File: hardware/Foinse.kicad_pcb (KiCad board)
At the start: 4 copper layers, 60 x 60 mm, 73 parts, among them J1 ESQ-110-X-X-D, J2 XT30PW-M, J4 PJ-002AH, J6 JTAG-10 PIN, U1 STM32F072C8Tx, U15 INA239AIDGSR, U16 INA239AIDGSR, U17 LTC4412xS6, U19 TPS56A37RPAR, U2 TLV70433DBVT, U4 TJA1051T-3, U5 TPS563203

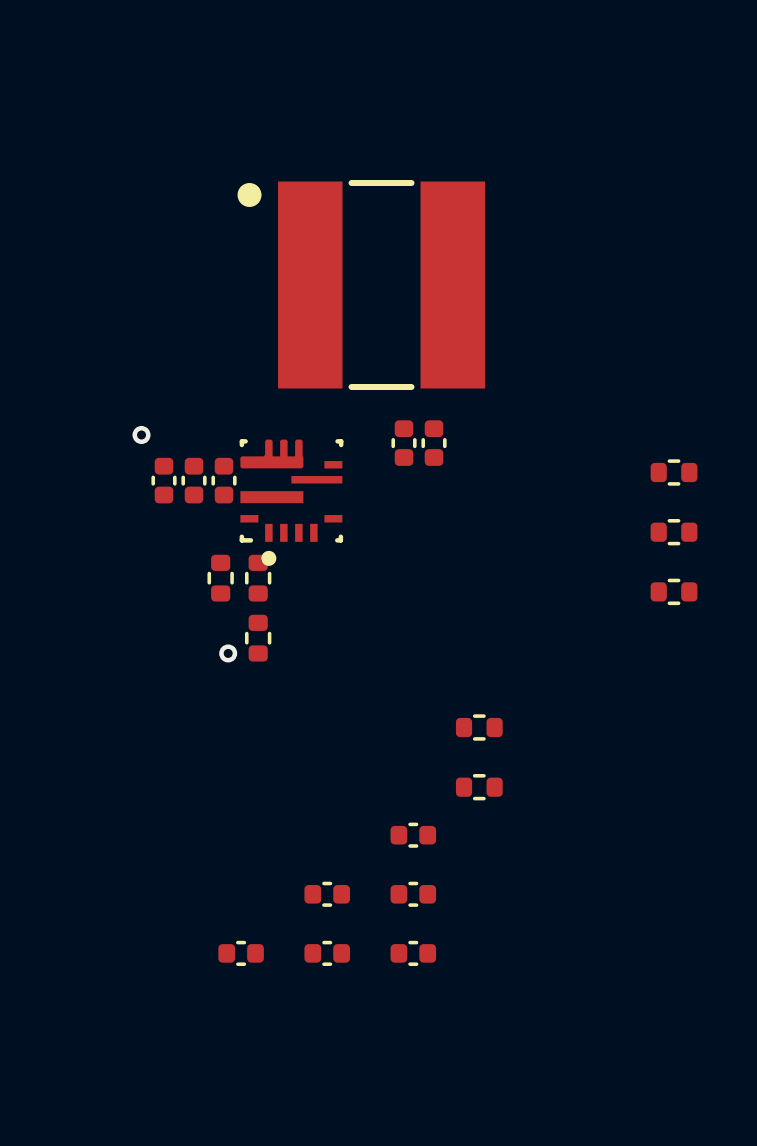
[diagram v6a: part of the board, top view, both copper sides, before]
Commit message: new inductor3
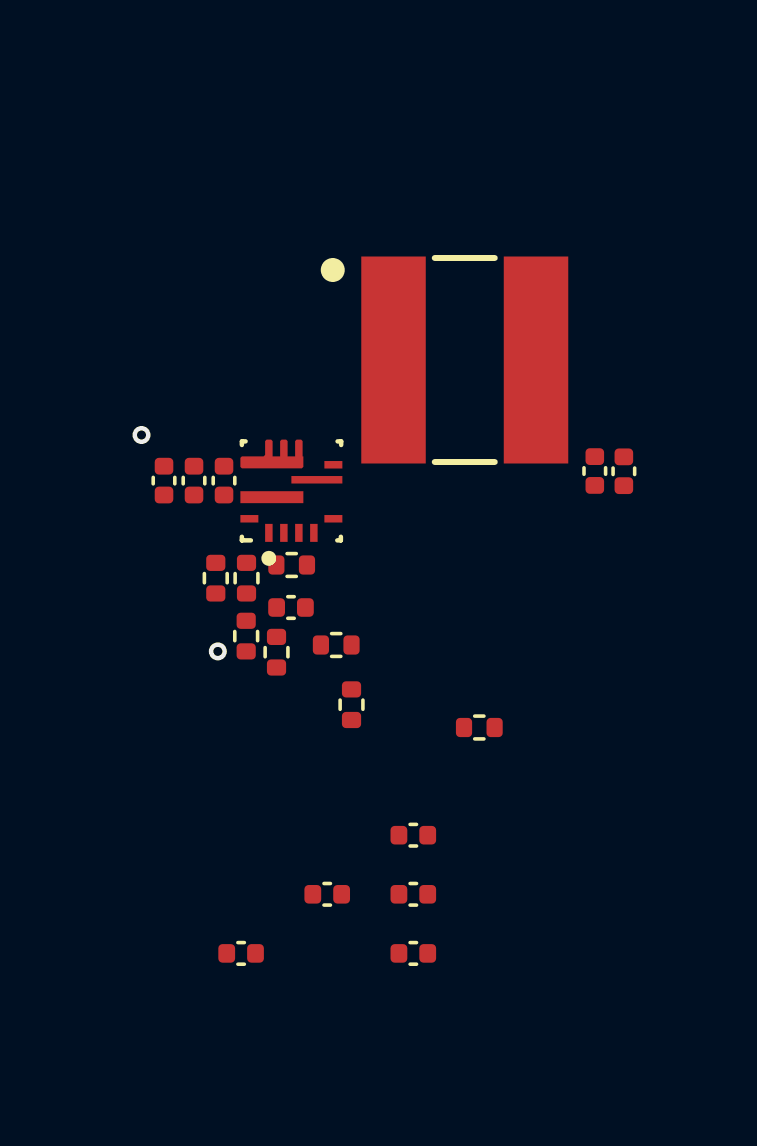
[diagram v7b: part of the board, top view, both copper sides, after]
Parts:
- moved R56 14.5 mm to (251.2, 69.2), turned to 90 degrees
- moved R58 12.8 mm to (251.8, 66.3)
- moved R57 11.9 mm to (253.2, 69.0)
- moved C41 11.6 mm to (251.7, 67.8), turned to 180 degrees
- moved C42 7.39 mm to (262.8, 63.2), turned to -90 degrees
- moved C43 5.44 mm to (261.9, 63.2), turned to -90 degrees
- moved R55 5.07 mm to (253.8, 71.0), turned to -90 degrees
- moved L1 3.74 mm to (257.5, 59.5)
- moved R52 0.41 mm to (250.2, 68.7)
- moved R53 0.39 mm to (250.2, 66.8)
- moved R51 0.16 mm to (249.2, 66.8)

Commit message: hehe
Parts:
- removed R54, R57: 0, Resistor_SMD:R_0402_1005Metric
- added R6: 10k Ω, Resistor_SMD:R_0402_1005Metric, F.Cu at (145.1, 94.2)
- moved R55 112.8 mm to (144.0, 97.0), turned to 90 degrees
- moved C42 111.9 mm to (154.3, 90.5)
- moved C43 111.9 mm to (153.4, 90.5)
- moved U19 111.9 mm to (143.2, 91.1)
- moved L1 111.9 mm to (149.0, 86.8)
- moved R52 111.9 mm to (142.0, 97.0)
- moved C37 111.8 mm to (141.0, 90.5)
- moved C38 111.8 mm to (139.0, 90.5)
- moved C39 111.8 mm to (140.0, 90.5)
- moved R51 111.8 mm to (140.9, 94.2)
- moved R53 111.8 mm to (141.9, 94.2)
- moved R56 111.7 mm to (143.0, 97.0)
- moved R58 111.7 mm to (143.5, 93.8)
- moved C41 111.6 mm to (143.6, 95.5)
- moved C40 108.9 mm to (144.6, 88.5), turned to 90 degrees
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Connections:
- C40 pad 1: Net-(C40-Pad1) -> Net-(U19-BOOT)
- R55 pad 2: Net-(R55-Pad2) -> Net-(C41-Pad1)
- R56 pad 1: Net-(R55-Pad2) -> Net-(C41-Pad1)
- U19 pad 4: unconnected-(U19-PG-Pad4) -> Net-(U19-PG)
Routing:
- net Net-(U19-EN): track 0.00 -> 4.81 mm
- net Net-(U19-FB): track 0.00 -> 3.70 mm
- net Net-(U19-SS): track 0.00 -> 2.65 mm
- net Net-(U19-MODE): track 0.00 -> 2.26 mm
- net Net-(U19-PG): track 0.00 -> 1.90 mm
- net GND: track 0.00 -> 1.51 mm, vias 7 -> 15
- net Net-(C41-Pad1): track 0.00 -> 1.02 mm
- net 5VSERVO_BS: vias 0 -> 2
